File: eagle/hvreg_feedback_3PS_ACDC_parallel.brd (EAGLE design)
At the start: 158.8 x 171.4 mm, 38 parts

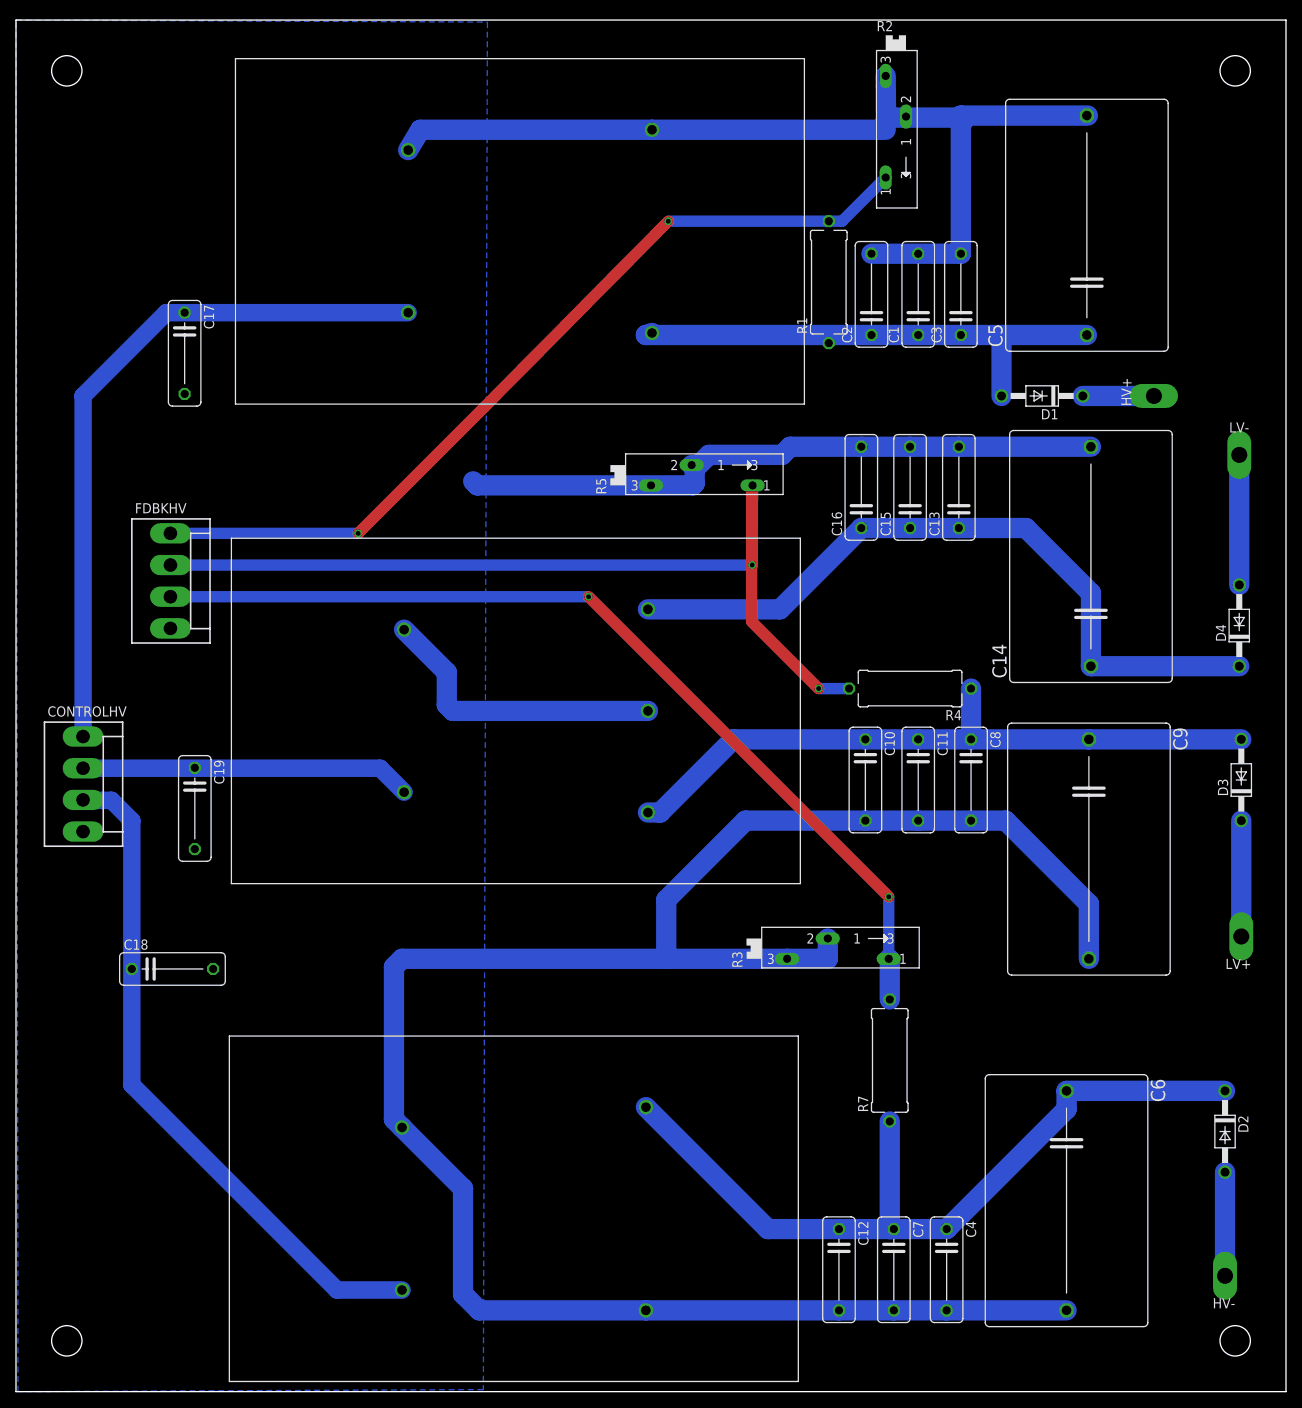
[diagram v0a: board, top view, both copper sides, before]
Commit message: two ps in parallel
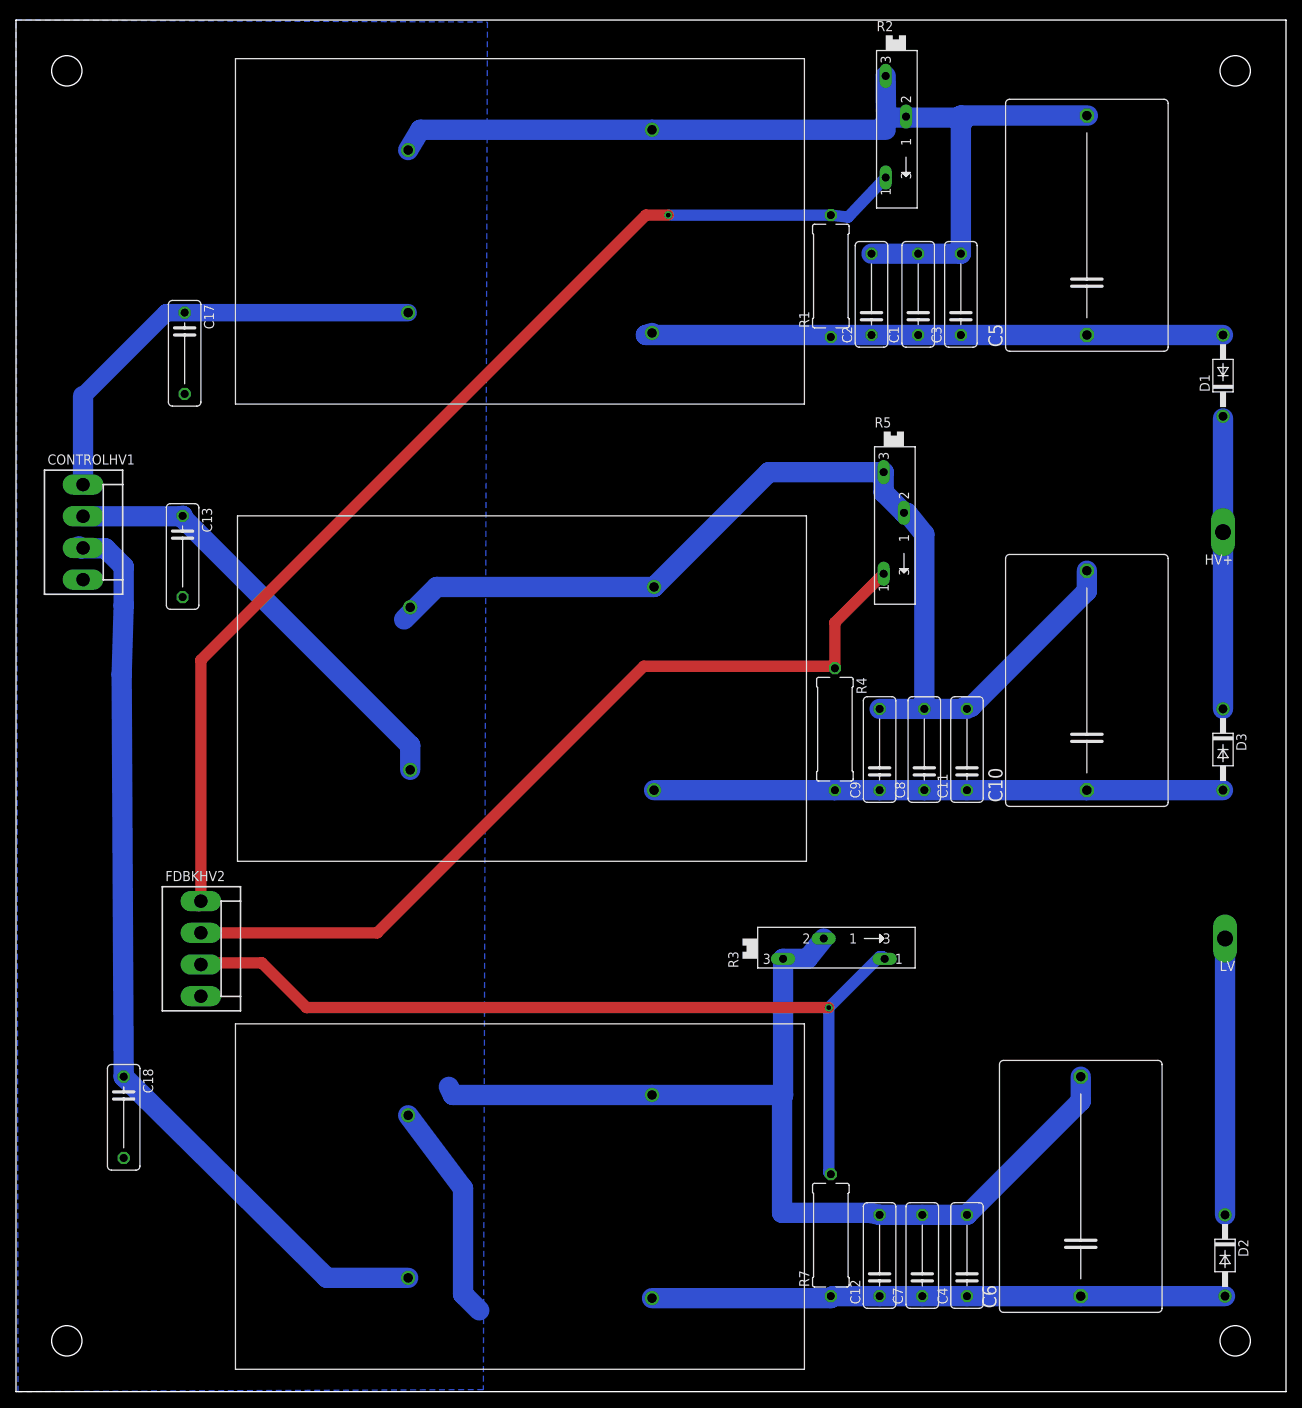
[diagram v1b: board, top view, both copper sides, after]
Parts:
- removed C14: 1u, rcl:C275-205X316
- removed C15: 1n, rcl:C102-043X133
- removed C16: 10p, rcl:C102-043X133
- removed C19: .1u, rcl:C102-043X133
- removed CONTROLHV, FDBKHV: (no value), con-molex:KK-156-4
- removed D4: 1N4004, diode:DO41-10
- removed HV-, LV+, LV-: TPPAD1-20Y, testpad:P1-20Y
- added CONTROLHV1, FDBKHV2: (no value), con-molex:KK-156-4
- added LV: TPPAD1-20Y, testpad:P1-20Y
- C10: value 1n -> 1u; device rcl:C102-043X133 -> rcl:C275-205X316
- C11: value 10p -> .01u
- C13: value .01u -> .1u
- C8: value .01u -> 1n
- C9: value 1u -> 10p; device rcl:C275-205X316 -> rcl:C102-043X133
- U$3: value EMCO-F20CT -> EMCO-F104PIN; device dc-dc-converter:EMCO-F*CT -> dc-dc-converter:EMCO-F
- moved C13 97.4 mm to (20.8, 104.4), turned to 270 degrees
- moved C10 30.4 mm to (133.9, 88.9), turned to 90 degrees
- moved C9 29.0 mm to (108.0, 80.3), turned to 90 degrees
- moved R5 24.3 mm to (109.7, 108.0), turned to 270 degrees
- moved R7 23.1 mm to (101.9, 19.6)
- moved D1 22.7 mm to (150.9, 127.0), turned to 90 degrees
- moved C18 19.5 mm to (13.5, 34.3), turned to 270 degrees
- moved HV+ 19.1 mm to (150.9, 107.4), turned to 180 degrees
- moved D2 15.5 mm to (151.1, 17.0)
- moved R4 10.7 mm to (102.4, 82.8), turned to 270 degrees
- moved C11 7.19 mm to (118.9, 80.3), turned to 90 degrees
- moved C8 6.97 mm to (113.5, 80.3), turned to 90 degrees
- moved C12 5.38 mm to (108.0, 17.0), turned to 90 degrees
- moved D3 4.44 mm to (150.9, 80.3), turned to 270 degrees
- moved C7 3.98 mm to (113.3, 17.0), turned to 90 degrees
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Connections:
- removed net N$12: D4.A, LV-.TP
- removed net N$14: C19.1, CONTROLHV.2, U$3.P$1
- removed net N$9: D3.C, LV+.TP
- net GND: now also CONTROLHV1.4, FDBKHV2.4, U$2.P$4, U$3.P$4; no longer C14.2, C15.2, C16.2, C19.2, CONTROLHV.4, FDBKHV.4, U$2.P$3, U$3.P$5
- net N$10: now also CONTROLHV1.2, U$3.P$1; no longer C14.1, C15.1, C16.1, D4.C, U$3.P$4
- net N$13: now also CONTROLHV1.1; no longer CONTROLHV.1
- net N$15: now also CONTROLHV1.3; no longer CONTROLHV.3
- net N$2: now also D2.A, U$2.P$3; no longer D2.C, U$2.P$4
- net N$3: now also FDBKHV2.1; no longer FDBKHV.1
- net N$4: now also D2.C, LV.TP; no longer D2.A, HV-.TP
- net N$5: now also FDBKHV2.2, R5.A; no longer C10.1, C11.1, C8.1, C9.1, D3.A, U$3.P$3
- net N$6: now also D3.C
- net N$7: now also C10.1, C11.1, C8.1, C9.1, D3.A, U$3.P$3; no longer FDBKHV.2, R5.A
- net N$8: now also FDBKHV2.3; no longer FDBKHV.3
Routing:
- net GND: track 493.8 -> 411.2 mm
- net N$7: track 115.4 -> 71.1 mm, vias 3 -> 0
- net N$14: track 41.4 -> 0.00 mm
- net N$10: track 90.6 -> 56.0 mm
- net N$3: track 107.9 -> 141.6 mm, vias 2 -> 1
- net N$15: track 84.6 -> 116.3 mm
- net N$13: track 87.5 -> 56.0 mm
- net N$2: track 100.7 -> 71.7 mm
- net N$6: track 10.2 -> 35.8 mm
- net N$5: track 84.3 -> 107.4 mm
- net N$4: track 13.0 -> 34.5 mm
- net N$12: track 16.3 -> 0.00 mm
- net N$9: track 14.5 -> 0.00 mm
- net N$1: track 63.0 -> 72.9 mm
- net N$8: track 118.2 -> 112.2 mm, vias 2 -> 1

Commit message: ultra layout. try that next time with lm317 interface
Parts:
- removed R4: 2M, resistor:P0613/15
- removed R5: (no value), pot:SP19L
- moved D1 7.74 mm to (145.8, 121.2), turned to 180 degrees
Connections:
- removed net N$5: FDBKHV2.2, R4.1, R5.A
- net GND: no longer R5.E, R5.S
- net N$1: no longer R1.1
- net N$3: now also FDBKHV2.2
- net N$6: now also R1.1
- net N$7: no longer R4.2
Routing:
- net N$5: track 107.4 -> 0.00 mm
- net N$1: track 72.9 -> 0.80 mm
- net N$7: track 71.1 -> 42.9 mm
- net GND: track 411.2 -> 390.3 mm
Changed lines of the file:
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@@
 <element name="C4" library="rcl" package="C102-043X133" value="1n" x="118.872" y="17.018" rot="R90"/>
 <element name="C7" library="rcl" package="C102-043X133" value="10p" x="113.284" y="17.018" rot="R90"/>
-<element name="D1" library="diode" package="DO41-10" value="1N4004" x="150.876" y="127" rot="R90"/>
 <element name="C17" library="rcl" package="C102-043X133" value=".1u" x="21.082" y="129.794" rot="R270"/>
 <element name="C18" library="rcl" package="C102-043X133" value=".1u" x="13.462" y="34.29" rot="R270"/>
@@
 <element name="C10" library="rcl" package="C275-205X316" value="1u" x="133.858" y="88.9" rot="R90"/>
 <element name="C11" library="rcl" package="C102-043X133" value=".01u" x="118.872" y="80.264" rot="R90"/>
-<element name="R4" library="resistor" package="P0613/15" value="2M" x="102.362" y="82.804" rot="R270"/>
 <element name="FDBKHV2" library="con-molex" package="KK-156-4" value="" x="23.114" y="55.372" rot="R270">
 <attribute name="OC_NEWARK" value="unknown" x="23.114" y="55.372" size="1.778" layer="27" rot="R270" display="off"/>
@@
 <attribute name="OC_FARNELL" value="unknown" x="23.114" y="55.372" size="1.778" layer="27" rot="R270" display="off"/>
 </element>
-<element name="R5" library="pot" package="SP19L" value="" x="109.728" y="107.95" rot="R270"/>
+<element name="D1" library="diode" package="DO41-10" value="1N4004" x="145.796" y="121.158" rot="R180"/>
 </elements>
 <signals>
@@
 <contactref element="C9" pad="2"/>
 <contactref element="FDBKHV2" pad="4"/>
-<contactref element="R5" pad="E"/>
-<contactref element="R5" pad="S"/>
 <wire x1="79.756" y1="100.584" x2="52.578" y2="100.584" width="2.54" layer="16"/>
 <wire x1="52.578" y1="100.584" x2="48.514" y2="96.52" width="2.54" layer="16"/>
@@
 <wire x1="133.096" y1="39.37" x2="133.096" y2="36.322" width="2.54" layer="16"/>
 <wire x1="133.096" y1="36.322" x2="118.872" y2="22.098" width="2.54" layer="16"/>
-<wire x1="108.458" y1="114.935" x2="108.458" y2="112.395" width="2.54" layer="16"/>
-<wire x1="108.458" y1="112.395" x2="110.998" y2="109.855" width="2.54" layer="16"/>
-<wire x1="110.998" y1="109.855" x2="111.379" y2="109.855" width="2.54" layer="16"/>
 <wire x1="111.379" y1="109.855" x2="113.538" y2="107.188" width="2.54" layer="16"/>
 <wire x1="113.538" y1="107.188" x2="113.538" y2="85.344" width="2.54" layer="16"/>
@@
 <wire x1="119.38" y1="85.598" x2="118.618" y2="85.598" width="2.54" layer="16"/>
 <wire x1="118.618" y1="85.598" x2="118.364" y2="85.344" width="2.54" layer="16"/>
-<wire x1="108.458" y1="114.935" x2="94.107" y2="114.935" width="2.54" layer="16"/>
 <wire x1="94.107" y1="114.935" x2="79.756" y2="100.584" width="2.54" layer="16"/>
-<wire x1="133.985" y1="159.512" x2="133.858" y2="159.512" width="0" layer="19" extent="16-16"/>
-<wire x1="108.712" y1="157.734" x2="108.458" y2="158.115" width="0" layer="19" extent="16-16"/>
+<wire x1="94.107" y1="114.935" x2="111.379" y2="109.855" width="0" layer="19" extent="16-16"/>
+<wire x1="108.458" y1="158.115" x2="108.712" y2="157.734" width="0" layer="19" extent="16-16"/>
+<wire x1="133.858" y1="159.512" x2="133.985" y2="159.512" width="0" layer="19" extent="16-16"/>
 <wire x1="111.252" y1="159.385" x2="109.284921875" y2="159.258" width="0" layer="19" extent="16-16"/>
 <wire x1="112.776" y1="142.24" x2="118.11" y2="142.24" width="0" layer="19" extent="1-1"/>
@@
 <contactref element="U$1" pad="P$3"/>
 <contactref element="C3" pad="1"/>
-<contactref element="R1" pad="1"/>
 <contactref element="C5" pad="1"/>
 <contactref element="C1" pad="1"/>
 <contactref element="C2" pad="1"/>
+<wire x1="78.74" y1="132.08" x2="79.502" y2="132.334" width="2.54" layer="16"/>
 <contactref element="D1" pad="A"/>
-<wire x1="133.858" y1="132.08" x2="78.74" y2="132.08" width="2.54" layer="16"/>
-<wire x1="78.74" y1="132.08" x2="79.502" y2="132.334" width="2.54" layer="16"/>
-<wire x1="150.876" y1="132.08" x2="133.858" y2="132.08" width="2.54" layer="16"/>
 <wire x1="112.776" y1="132.08" x2="118.11" y2="132.08" width="0" layer="19" extent="1-1"/>
 <wire x1="106.934" y1="132.08" x2="112.776" y2="132.08" width="0" layer="19" extent="1-1"/>
-<wire x1="101.854" y1="131.826" x2="106.934" y2="132.08" width="0" layer="19" extent="1-1"/>
 <wire x1="133.858" y1="132.08" x2="118.11" y2="132.08" width="0" layer="19" extent="1-1"/>
+<wire x1="140.716" y1="121.158" x2="133.858" y2="132.08" width="0" layer="19" extent="1-1"/>
+<wire x1="79.502" y1="132.334" x2="106.934" y2="132.08" width="0" layer="19" extent="1-1"/>
 </signal>
 <signal name="N$2">
@@
 <wire x1="23.114" y1="91.44" x2="23.114" y2="60.96" width="1.4224" layer="1"/>
 <wire x1="23.114" y1="60.96" x2="22.86" y2="60.706" width="1.4224" layer="1"/>
-<wire x1="22.86" y1="60.706" x2="23.114" y2="61.312" width="0" layer="19" extent="1-16"/>
+<contactref element="FDBKHV2" pad="2"/>
+<wire x1="23.114" y1="60.96" x2="23.114" y2="61.312" width="0" layer="19" extent="1-1"/>
+<wire x1="23.114" y1="57.352" x2="22.86" y2="60.706" width="0" layer="19" extent="1-1"/>
 </signal>
 <signal name="N$8">
@@
 </signal>
 <signal name="N$6">
-<contactref element="D1" pad="C"/>
 <contactref element="HV+" pad="TP"/>
 <contactref element="D3" pad="C"/>
 <wire x1="150.876" y1="85.344" x2="150.876" y2="106.934" width="2.54" layer="16"/>
 <wire x1="150.876" y1="107.442" x2="150.876" y2="121.666" width="2.54" layer="16"/>
-<wire x1="150.876" y1="121.666" x2="150.876" y2="121.92" width="0" layer="19" extent="16-16"/>
+<contactref element="D1" pad="C"/>
+<contactref element="R1" pad="1"/>
+<wire x1="150.876" y1="121.666" x2="101.854" y2="131.826" width="0" layer="19" extent="16-16"/>
+<wire x1="150.876" y1="121.158" x2="150.876" y2="121.666" width="0" layer="19" extent="16-16"/>
 <wire x1="150.876" y1="106.934" x2="150.876" y2="107.442" width="0" layer="19" extent="16-16"/>
 </signal>
@@
 <contactref element="C10" pad="1"/>
 <contactref element="U$3" pad="P$3"/>
-<contactref element="R4" pad="2"/>
-<wire x1="79.756" y1="75.184" x2="102.362" y2="75.184" width="2.54" layer="16"/>
-<wire x1="102.362" y1="75.184" x2="107.95" y2="75.184" width="2.54" layer="16"/>
 <wire x1="107.95" y1="75.184" x2="113.538" y2="75.184" width="2.54" layer="16"/>
 <wire x1="113.538" y1="75.184" x2="118.872" y2="75.184" width="2.54" layer="16"/>
 <wire x1="118.872" y1="75.184" x2="133.858" y2="75.184" width="2.54" layer="16"/>
 <wire x1="133.858" y1="75.184" x2="150.876" y2="75.184" width="2.54" layer="16"/>
-</signal>
-<signal name="N$5">
-<contactref element="R4" pad="1"/>
-<contactref element="FDBKHV2" pad="2"/>
-<contactref element="R5" pad="A"/>
-<wire x1="23.114" y1="57.352" x2="45.16" y2="57.352" width="1.4224" layer="1"/>
-<wire x1="45.16" y1="57.352" x2="78.486" y2="90.678" width="1.4224" layer="1"/>
-<wire x1="78.486" y1="90.678" x2="101.854" y2="90.678" width="1.4224" layer="1"/>
-<wire x1="101.854" y1="90.678" x2="102.362" y2="90.424" width="1.4224" layer="1"/>
-<wire x1="102.362" y1="90.424" x2="102.362" y2="96.139" width="1.4224" layer="1"/>
-<wire x1="102.362" y1="96.139" x2="108.458" y2="102.235" width="1.4224" layer="1"/>
+<wire x1="79.756" y1="75.184" x2="107.95" y2="75.184" width="0" layer="19" extent="1-1"/>
 </signal>
 </signals>
